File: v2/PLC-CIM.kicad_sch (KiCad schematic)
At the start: 0 parts

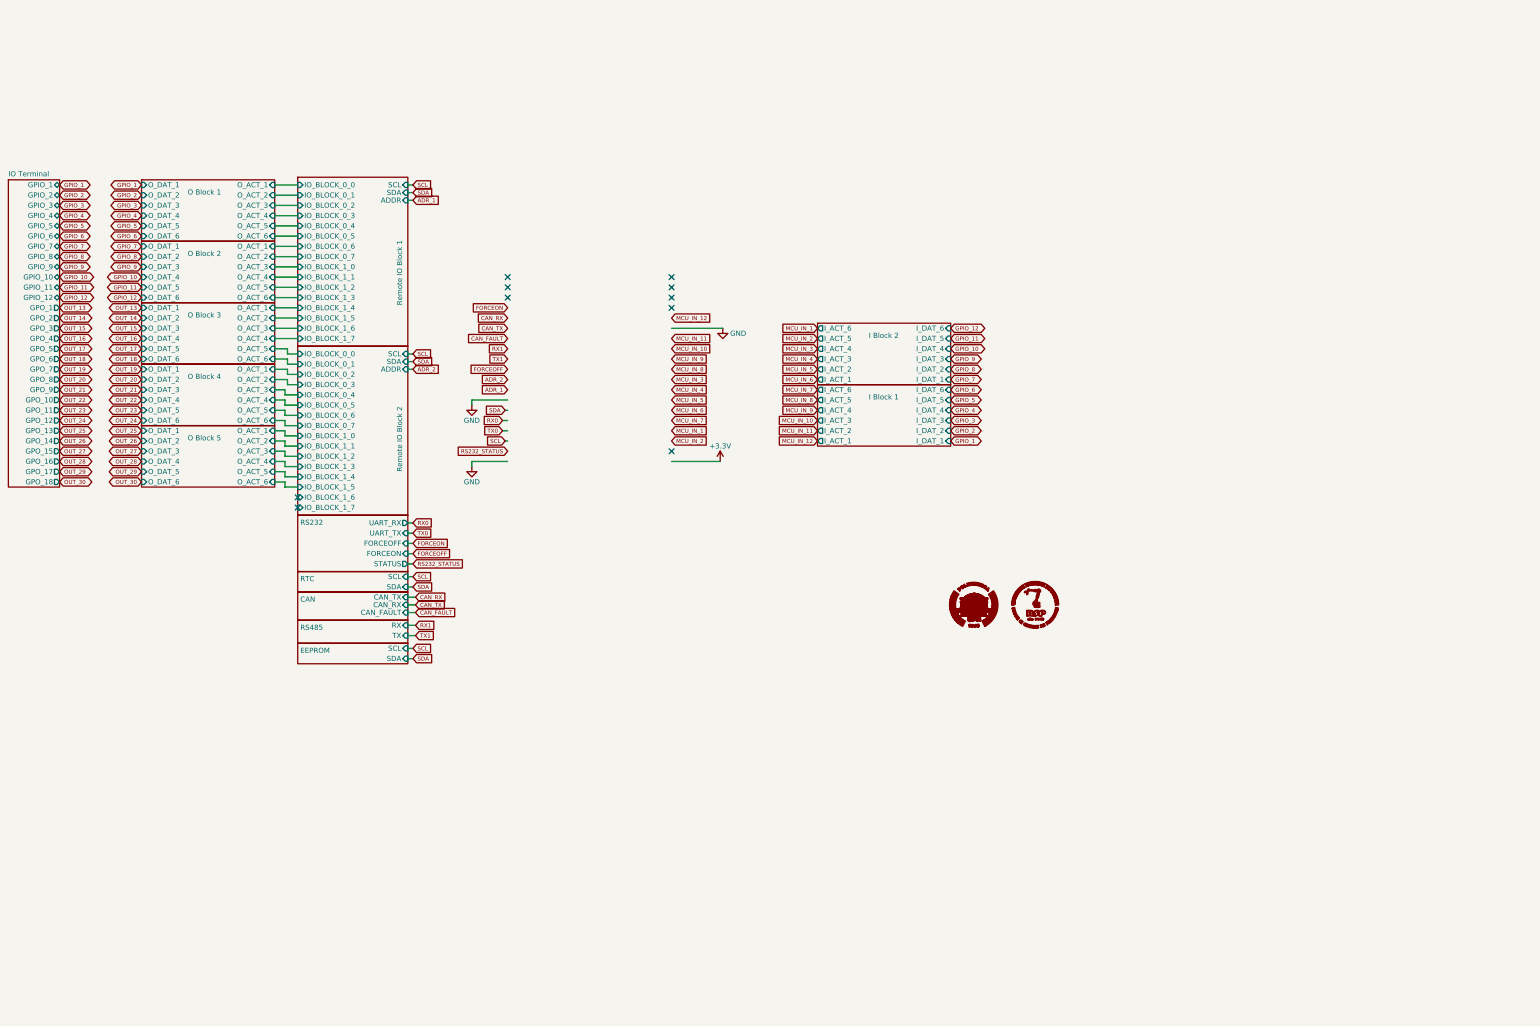
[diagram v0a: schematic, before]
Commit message: Start proper work on V2.1
- Replaced all blocks
- Added input blocks
- Added output blocks
- Added initial CAD placement
- Added initial routing
- General system stability improvements to enhance the user's experience
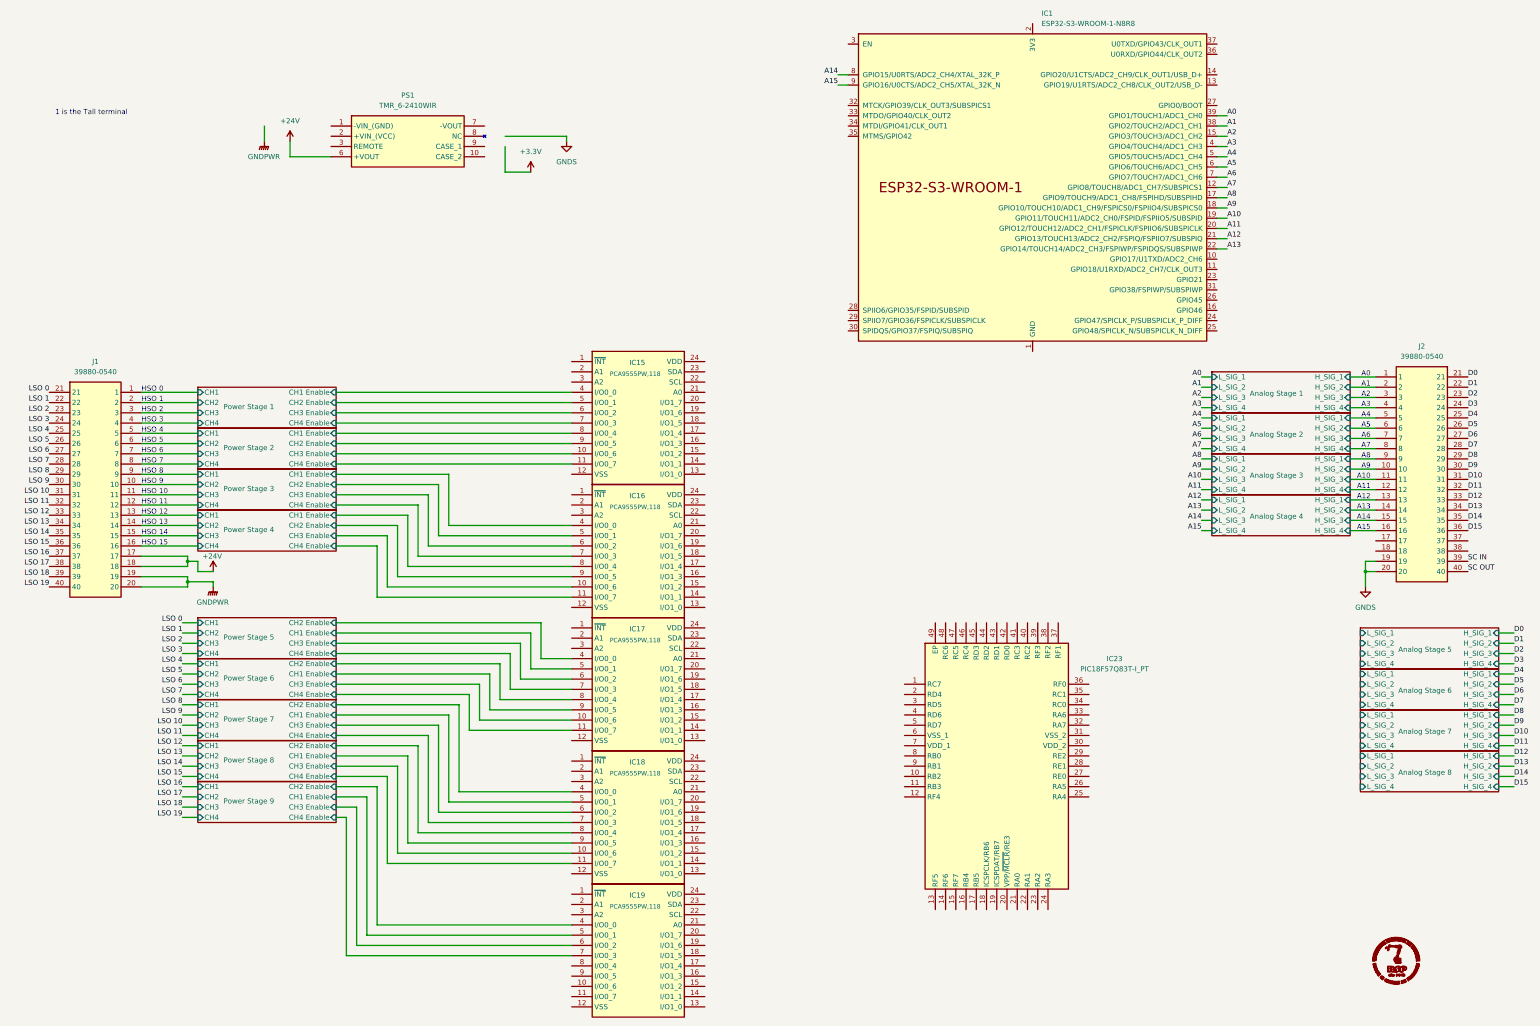
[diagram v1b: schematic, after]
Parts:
- added IC1: ESP32-S3-WROOM-1-N8R8, mod:ESP32S3WROOM1N8R8, symbol Espressif:ESP32-S3-WROOM-1
- added IC15, IC16, IC17, IC18, IC19: PCA9555PW,118, mod:SOP65P640X110-24N, symbol PCA9555PW_118:PCA9555PW,118
- added IC23: PIC18F57Q83T-I_PT, mod:QFP50P900X900X120-49N, symbol PIC18F57Q83T-I_PT:PIC18F57Q83T-I_PT
- added J1, J2: 39880-0540, mod:398800540, symbol 39880-0540:39880-0540
- added PS1: TMR_6-2410WIR, TMR62410WIR, symbol TMR_6-2410WIR:TMR_6-2410WIR
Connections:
- new net: IC1.1 (GND), IC1.40 (GND), IC1.41 (GND)
- new net +24V: J1.17, J1.18, PS1.6 (+VOUT)
- new net A0: IC1.39 (GPIO1/TOUCH1/ADC1_CH0)
- new net A1: IC1.38 (GPIO2/TOUCH2/ADC1_CH1)
- new net A10: IC1.19 (GPIO11/TOUCH11/ADC2_CH0/FSPID/FSPIIO5/SUBSPID)
- new net A11: IC1.20 (GPIO12/TOUCH12/ADC2_CH1/FSPICLK/FSPIIO6/SUBSPICLK)
- new net A12: IC1.21 (GPIO13/TOUCH13/ADC2_CH2/FSPIQ/FSPIIO7/SUBSPIQ)
- new net A13: IC1.22 (GPIO14/TOUCH14/ADC2_CH3/FSPIWP/FSPIDQS/SUBSPIWP)
- new net A14: IC1.8 (GPIO15/U0RTS/ADC2_CH4/XTAL_32K_P)
- new net A15: IC1.9 (GPIO16/U0CTS/ADC2_CH5/XTAL_32K_N)
- new net A2: IC1.15 (GPIO3/TOUCH3/ADC1_CH2)
- new net A3: IC1.4 (GPIO4/TOUCH4/ADC1_CH3)
- new net A4: IC1.5 (GPIO5/TOUCH5/ADC1_CH4)
- new net A5: IC1.6 (GPIO6/TOUCH6/ADC1_CH5)
- new net A6: IC1.7 (GPIO7/TOUCH7/ADC1_CH6)
- new net A7: IC1.12 (GPIO8/TOUCH8/ADC1_CH7/SUBSPICS1)
- new net A8: IC1.17 (GPIO9/TOUCH9/ADC1_CH8/FSPIHD/SUBSPIHD)
- new net A9: IC1.18 (GPIO10/TOUCH10/ADC1_CH9/FSPICS0/FSPIIO4/SUBSPICS0)
- new net Analog Stage 1/H_SIG_1: J2.1
- new net Analog Stage 1/H_SIG_2: J2.2
- new net Analog Stage 1/H_SIG_3: J2.3
- new net Analog Stage 1/H_SIG_4: J2.4
- new net Analog Stage 2/H_SIG_1: J2.5
- new net Analog Stage 2/H_SIG_2: J2.6
- new net Analog Stage 2/H_SIG_3: J2.7
- new net Analog Stage 2/H_SIG_4: J2.8
- new net Analog Stage 3/H_SIG_1: J2.9
- new net Analog Stage 3/H_SIG_2: J2.10
- new net Analog Stage 3/H_SIG_3: J2.11
- new net Analog Stage 3/H_SIG_4: J2.12
- new net Analog Stage 4/H_SIG_1: J2.13
- new net Analog Stage 4/H_SIG_2: J2.14
- new net Analog Stage 4/H_SIG_3: J2.15
- new net Analog Stage 4/H_SIG_4: J2.16
- new net D0: J2.21
- new net D1: J2.22
- new net D10: J2.31
- new net D11: J2.32
- new net D12: J2.33
- new net D13: J2.34
- new net D14: J2.35
- new net D15: J2.36
- new net D2: J2.23
- new net D3: J2.24
- new net D4: J2.25
- new net D5: J2.26
- new net D6: J2.27
- new net D7: J2.28
- new net D8: J2.29
- new net D9: J2.30
- new net GNDPWR: J1.19, J1.20
- new net GNDS: J2.19, J2.20
- new net LSO 0: J1.21
- new net LSO 1: J1.22
- new net LSO 10: J1.31
- new net LSO 11: J1.32
- new net LSO 12: J1.33
- new net LSO 13: J1.34
- new net LSO 14: J1.35
- new net LSO 15: J1.36
- new net LSO 16: J1.37
- new net LSO 17: J1.38
- new net LSO 18: J1.39
- new net LSO 19: J1.40
- new net LSO 2: J1.23
- new net LSO 3: J1.24
- new net LSO 4: J1.25
- new net LSO 5: J1.26
- new net LSO 6: J1.27
- new net LSO 7: J1.28
- new net LSO 8: J1.29
- new net LSO 9: J1.30
- new net Power Stage 1/CH1: J1.1
- new net Power Stage 1/CH1 Enable: IC15.4 (I/O0_0)
- new net Power Stage 1/CH2: J1.2
- new net Power Stage 1/CH2 Enable: IC15.5 (I/O0_1)
- new net Power Stage 1/CH3: J1.3
- new net Power Stage 1/CH3 Enable: IC15.6 (I/O0_2)
- new net Power Stage 1/CH4: J1.4
- new net Power Stage 1/CH4 Enable: IC15.7 (I/O0_3)
- new net Power Stage 2/CH1: J1.5
- new net Power Stage 2/CH1 Enable: IC15.8 (I/O0_4)
- new net Power Stage 2/CH2: J1.6
- new net Power Stage 2/CH2 Enable: IC15.9 (I/O0_5)
- new net Power Stage 2/CH3: J1.7
- new net Power Stage 2/CH3 Enable: IC15.10 (I/O0_6)
- new net Power Stage 2/CH4: J1.8
- new net Power Stage 2/CH4 Enable: IC15.11 (I/O0_7)
- new net Power Stage 3/CH1: J1.9
- new net Power Stage 3/CH1 Enable: IC16.4 (I/O0_0)
- new net Power Stage 3/CH2: J1.10
- new net Power Stage 3/CH2 Enable: IC16.5 (I/O0_1)
- new net Power Stage 3/CH3: J1.11
- new net Power Stage 3/CH3 Enable: IC16.6 (I/O0_2)
- new net Power Stage 3/CH4: J1.12
- new net Power Stage 3/CH4 Enable: IC16.7 (I/O0_3)
- new net Power Stage 4/CH1: J1.13
- new net Power Stage 4/CH1 Enable: IC16.8 (I/O0_4)
- new net Power Stage 4/CH2: J1.14
- new net Power Stage 4/CH2 Enable: IC16.9 (I/O0_5)
- new net Power Stage 4/CH3: J1.15
- new net Power Stage 4/CH3 Enable: IC16.10 (I/O0_6)
- new net Power Stage 4/CH4: J1.16
- new net Power Stage 4/CH4 Enable: IC16.11 (I/O0_7)
- new net Power Stage 5/CH1 Enable: IC17.5 (I/O0_1)
- new net Power Stage 5/CH2 Enable: IC17.4 (I/O0_0)
- new net Power Stage 5/CH3 Enable: IC17.6 (I/O0_2)
- new net Power Stage 5/CH4 Enable: IC17.7 (I/O0_3)
- new net Power Stage 6/CH1 Enable: IC17.9 (I/O0_5)
- new net Power Stage 6/CH2 Enable: IC17.8 (I/O0_4)
- new net Power Stage 6/CH3 Enable: IC17.10 (I/O0_6)
- new net Power Stage 6/CH4 Enable: IC17.11 (I/O0_7)
- new net Power Stage 7/CH1 Enable: IC18.5 (I/O0_1)
- new net Power Stage 7/CH2 Enable: IC18.4 (I/O0_0)
- new net Power Stage 7/CH3 Enable: IC18.6 (I/O0_2)
- new net Power Stage 7/CH4 Enable: IC18.7 (I/O0_3)
- new net Power Stage 8/CH1 Enable: IC18.9 (I/O0_5)
- new net Power Stage 8/CH2 Enable: IC18.8 (I/O0_4)
- new net Power Stage 8/CH3 Enable: IC18.10 (I/O0_6)
- new net Power Stage 8/CH4 Enable: IC18.11 (I/O0_7)
- new net Power Stage 9/CH1 Enable: IC19.5 (I/O0_1)
- new net Power Stage 9/CH2 Enable: IC19.4 (I/O0_0)
- new net Power Stage 9/CH3 Enable: IC19.6 (I/O0_2)
- new net Power Stage 9/CH4 Enable: IC19.7 (I/O0_3)
- new net SC IN: J2.39
- new net SC OUT: J2.40
- no-connect marks 10 -> 0
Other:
- removed sheet CAN
- removed sheet EEPROM
- removed sheet I Block 1
- removed sheet I Block 2
- removed sheet IO Terminal
- removed sheet O Block 1
- removed sheet O Block 2
- removed sheet O Block 3
- removed sheet O Block 4
- removed sheet O Block 5
- removed sheet RS232
- removed sheet RS485
- removed sheet RTC
- removed sheet Remote IO Block 1
- removed sheet Remote IO Block 2
- added sheet Analog Stage 1 (Blocks/ASS.kicad_sch)
- added sheet Analog Stage 2 (Blocks/ASS.kicad_sch)
- added sheet Analog Stage 3 (Blocks/ASS.kicad_sch)
- added sheet Analog Stage 4 (Blocks/ASS.kicad_sch)
- added sheet Analog Stage 5 (Blocks/ASS.kicad_sch)
- added sheet Analog Stage 6 (Blocks/ASS.kicad_sch)
- added sheet Analog Stage 7 (Blocks/ASS.kicad_sch)
- added sheet Analog Stage 8 (Blocks/ASS.kicad_sch)
- added sheet Power Stage 1 (Blocks/PS.kicad_sch)
- added sheet Power Stage 2 (Blocks/PS.kicad_sch)
- added sheet Power Stage 3 (Blocks/PS.kicad_sch)
- added sheet Power Stage 4 (Blocks/PS.kicad_sch)
- added sheet Power Stage 5 (Blocks/PS.kicad_sch)
- added sheet Power Stage 6 (Blocks/PS.kicad_sch)
- added sheet Power Stage 7 (Blocks/PS.kicad_sch)
- added sheet Power Stage 8 (Blocks/PS.kicad_sch)
- added sheet Power Stage 9 (Blocks/PS.kicad_sch)
- note added: "1 is the Tall terminal"
- note added: "A0"
- note added: "A1"
- note added: "A10"
- note added: "A11"
- note added: "A12"
- note added: "A13"
- note added: "A14"
- note added: "A15"
- note added: "A2"
- note added: "A3"
- note added: "A4"
- note added: "A5"
- note added: "A6"
- note added: "A7"
- note added: "A8"
- note added: "A9"
- note added: "HSO 0"
- note added: "HSO 1"
- note added: "HSO 10"
- note added: "HSO 11"
- note added: "HSO 12"
- note added: "HSO 13"
- note added: "HSO 14"
- note added: "HSO 15"
- note added: "HSO 2"
- note added: "HSO 3"
- note added: "HSO 4"
- note added: "HSO 5"
- note added: "HSO 6"
- note added: "HSO 7"
- note added: "HSO 8"
- note added: "HSO 9"
